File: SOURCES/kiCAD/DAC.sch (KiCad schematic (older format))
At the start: 196 parts, among them J16 MJ-519, J17 MJ-519, J20 MJ-519, J21 MJ-519, J24 Conn_01x06, J25 Conn_01x06, J27 Conn_01x06, J28 Conn_01x06, Q10 2SC3326, Q11 2SC3326, Q15 2SC3326, Q16 2SC3326, Q17 2SC3326, Q18 2SC3326, Q19 2SC3326, Q20 2SC3326, Q21 2SC3326, Q22 2SC3326, Q23 2SC3326, Q24 2SC3326, Q25 2SC3326, Q26 2SC3326, Q27 2SC3326, Q28 2SC3326, U14 PCM5102A, U16 PCM5102A, U17 PCM5102A, U18 PCM5102A, U20 OPA1632DR, U21 OPA1632DR, U22 OPA1632DR, U23 OPA1632DR, U24 OPA1632DR, U25 OPA1632DR, U26 OPA1632DR, U27 OPA1632DR

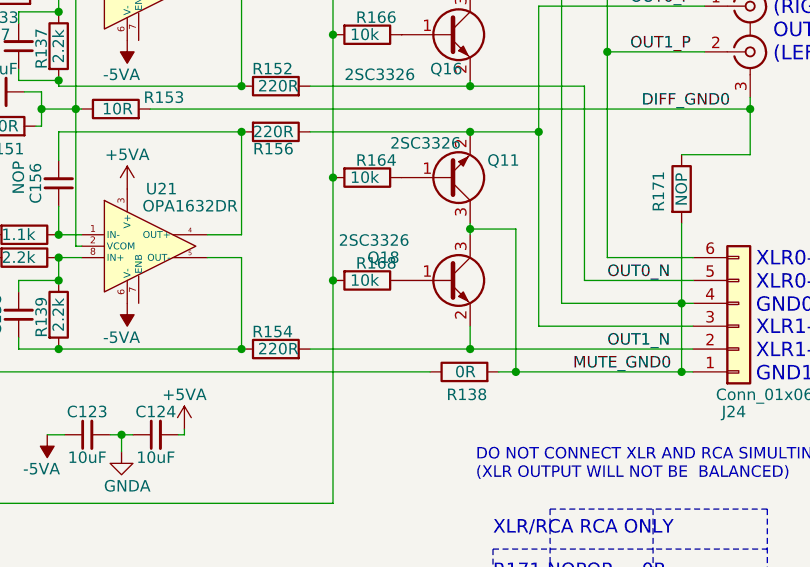
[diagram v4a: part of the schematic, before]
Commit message: Improved Coax Input Noise Immunities
Changed Coax input amp design and AC couling to EXOR
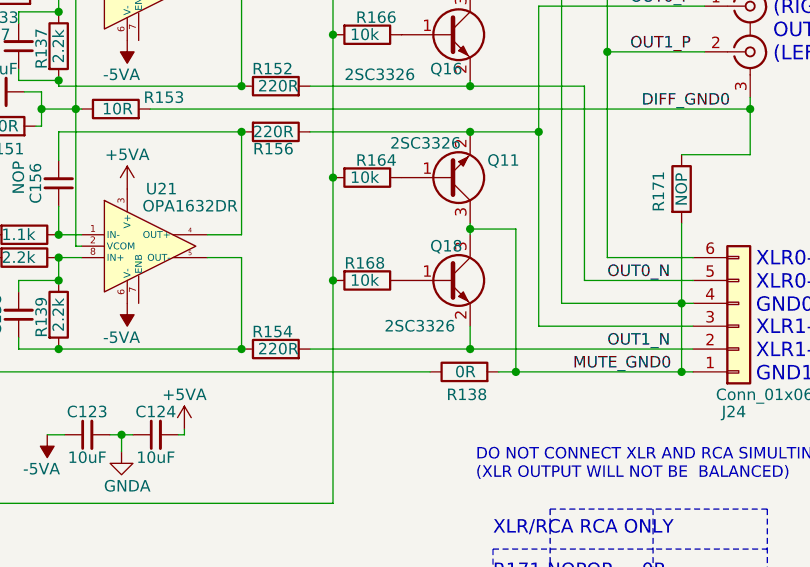
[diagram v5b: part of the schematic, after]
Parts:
- C114, C115, C116, C117, C96, C97, C98, C99: Description se Audio-Grade or Film Cap (ie. PML, ECHU, etc..) -> Use Audio-Grade or Film Cap (ie. PML, ECHU, etc..)
- C144, C146, C150, C151, C157, C158, C160, C161: Description use Audio-Grade or Film Cap (ie. PML, ECHU, etc..) -> Use Audio-Grade or Film Cap (ie. PML, ECHU, etc..); JLPCB# C363520 -> C525291
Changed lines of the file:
@@
 Title "FreeDSP OCTAVIA DAC part"
 Date "2023-07-22"
-Rev "0.3"
+Rev "0.32"
 Comp ""
 Comment1 ""
@@
 F 3 "~" H 11025 2875 50  0001 C CNN
 F 4 "C342877" H 11025 2875 50  0001 C CNN "JLPCB#"
-F 5 "se Audio-Grade or Film Cap (ie. PML, ECHU, etc..)" H 11025 2875 50  0001 C CNN "Description"
+F 5 "Use Audio-Grade or Film Cap (ie. PML, ECHU, etc..)" H 11025 2875 50  0001 C CNN "Description"
 	1    11025 2875
 	1    0    0    1
@@
 F 3 "~" H 11175 2875 50  0001 C CNN
 F 4 "C342877" H 11175 2875 50  0001 C CNN "JLPCB#"
-F 5 "se Audio-Grade or Film Cap (ie. PML, ECHU, etc..)" H 11175 2875 50  0001 C CNN "Description"
+F 5 "Use Audio-Grade or Film Cap (ie. PML, ECHU, etc..)" H 11175 2875 50  0001 C CNN "Description"
 	1    11175 2875
 	1    0    0    1
@@
 F 3 "~" H 3550 6900 50  0001 C CNN
 F 4 "C342877" H 3550 6900 50  0001 C CNN "JLPCB#"
-F 5 "se Audio-Grade or Film Cap (ie. PML, ECHU, etc..)" H 3550 6900 50  0001 C CNN "Description"
+F 5 "Use Audio-Grade or Film Cap (ie. PML, ECHU, etc..)" H 3550 6900 50  0001 C CNN "Description"
 	1    3550 6900
 	1    0    0    1
@@
 F 3 "~" H 3700 6900 50  0001 C CNN
 F 4 "C342877" H 3700 6900 50  0001 C CNN "JLPCB#"
-F 5 "se Audio-Grade or Film Cap (ie. PML, ECHU, etc..)" H 3700 6900 50  0001 C CNN "Description"
+F 5 "Use Audio-Grade or Film Cap (ie. PML, ECHU, etc..)" H 3700 6900 50  0001 C CNN "Description"
 	1    3700 6900
 	1    0    0    1
@@
 F 3 "~" H 11150 6775 50  0001 C CNN
 F 4 "C342877" H 11150 6775 50  0001 C CNN "JLPCB#"
-F 5 "se Audio-Grade or Film Cap (ie. PML, ECHU, etc..)" H 11150 6775 50  0001 C CNN "Description"
+F 5 "Use Audio-Grade or Film Cap (ie. PML, ECHU, etc..)" H 11150 6775 50  0001 C CNN "Description"
 	1    11150 6775
 	1    0    0    1
@@
 F 3 "~" H 11300 6775 50  0001 C CNN
 F 4 "C342877" H 11300 6775 50  0001 C CNN "JLPCB#"
-F 5 "se Audio-Grade or Film Cap (ie. PML, ECHU, etc..)" H 11300 6775 50  0001 C CNN "Description"
+F 5 "Use Audio-Grade or Film Cap (ie. PML, ECHU, etc..)" H 11300 6775 50  0001 C CNN "Description"
 	1    11300 6775
 	1    0    0    1
@@
 AR Path="/5D902CF8/656EA003" Ref="R?"  Part="1"
 AR Path="/5D902CF8/65D81CA2/656EA003" Ref="R168"  Part="1"
-F 0 "R168" V 5625 3925 50  0000 L CNN
+F 0 "R168" V 5625 3875 50  0000 L CNN
 F 1 "10k" V 5700 3900 50  0000 L CNN
 F 2 "Resistor_SMD:R_0603_1608Metric" V 5630 3975 50  0001 C CNN
@@
 U 1 1 65507B78
 P 6050 3975
-F 0 "Q18" H 5700 4075 50  0000 L CNN
-F 1 "2SC3326" H 5575 4150 50  0000 L CNN
+F 0 "Q18" H 5975 4125 50  0000 L CNN
+F 1 "2SC3326" H 5775 3775 50  0000 L CNN
 F 2 "Package_TO_SOT_SMD:SOT-23" H 6250 4075 50  0001 C CNN
 F 3 "~" H 6050 3975 50  0001 C CNN
@@
 F 3 "~" H 3350 3075 50  0001 C CNN
 F 4 "C342877" H 3350 3075 50  0001 C CNN "JLPCB#"
-F 5 "se Audio-Grade or Film Cap (ie. PML, ECHU, etc..)" H 3350 3075 50  0001 C CNN "Description"
+F 5 "Use Audio-Grade or Film Cap (ie. PML, ECHU, etc..)" H 3350 3075 50  0001 C CNN "Description"
 	1    3350 3075
 	1    0    0    1
@@
 F 2 "Capacitor_SMD:C_0805_2012Metric_Pad1.18x1.45mm_HandSolder" H 12275 6700 50  0001 C CNN
 F 3 "~" H 12275 6700 50  0001 C CNN
-F 4 "C363520" H 12275 6700 50  0001 C CNN "JLPCB#"
-F 5 "use Audio-Grade or Film Cap (ie. PML, ECHU, etc..)" H 12275 6700 50  0001 C CNN "Description"
+F 4 "C525291" H 12275 6700 50  0001 C CNN "JLPCB#"
+F 5 "Use Audio-Grade or Film Cap (ie. PML, ECHU, etc..)" H 12275 6700 50  0001 C CNN "Description"
 	1    12275 6700
 	1    0    0    1
@@
 F 2 "Capacitor_SMD:C_0805_2012Metric_Pad1.18x1.45mm_HandSolder" H 12350 7850 50  0001 C CNN
 F 3 "~" H 12350 7850 50  0001 C CNN
-F 4 "C363520" H 12350 7850 50  0001 C CNN "JLPCB#"
-F 5 "use Audio-Grade or Film Cap (ie. PML, ECHU, etc..)" H 12350 7850 50  0001 C CNN "Description"
+F 4 "C525291" H 12350 7850 50  0001 C CNN "JLPCB#"
+F 5 "Use Audio-Grade or Film Cap (ie. PML, ECHU, etc..)" H 12350 7850 50  0001 C CNN "Description"
 	1    12350 7850
 	1    0    0    1
@@
 F 2 "Capacitor_SMD:C_0805_2012Metric_Pad1.18x1.45mm_HandSolder" H 12000 2800 50  0001 C CNN
 F 3 "~" H 12000 2800 50  0001 C CNN
-F 4 "C363520" H 12000 2800 50  0001 C CNN "JLPCB#"
-F 5 "use Audio-Grade or Film Cap (ie. PML, ECHU, etc..)" H 12000 2800 50  0001 C CNN "Description"
+F 4 "C525291" H 12000 2800 50  0001 C CNN "JLPCB#"
+F 5 "Use Audio-Grade or Film Cap (ie. PML, ECHU, etc..)" H 12000 2800 50  0001 C CNN "Description"
 	1    12000 2800
 	1    0    0    1
@@
 F 2 "Capacitor_SMD:C_0805_2012Metric_Pad1.18x1.45mm_HandSolder" H 12075 4050 50  0001 C CNN
 F 3 "~" H 12075 4050 50  0001 C CNN
-F 4 "C363520" H 12075 4050 50  0001 C CNN "JLPCB#"
-F 5 "use Audio-Grade or Film Cap (ie. PML, ECHU, etc..)" H 12075 4050 50  0001 C CNN "Description"
+F 4 "C525291" H 12075 4050 50  0001 C CNN "JLPCB#"
+F 5 "Use Audio-Grade or Film Cap (ie. PML, ECHU, etc..)" H 12075 4050 50  0001 C CNN "Description"
 	1    12075 4050
 	1    0    0    1
@@
 F 3 "~" H 3200 3075 50  0001 C CNN
 F 4 "C342877" H 3200 3075 50  0001 C CNN "JLPCB#"
-F 5 "se Audio-Grade or Film Cap (ie. PML, ECHU, etc..)" H 3200 3075 50  0001 C CNN "Description"
+F 5 "Use Audio-Grade or Film Cap (ie. PML, ECHU, etc..)" H 3200 3075 50  0001 C CNN "Description"
 	1    3200 3075
 	1    0    0    1
@@
 F 2 "Capacitor_SMD:C_0805_2012Metric_Pad1.18x1.45mm_HandSolder" H 4175 4125 50  0001 C CNN
 F 3 "~" H 4175 4125 50  0001 C CNN
-F 4 "C363520" H 4175 4125 50  0001 C CNN "JLPCB#"
-F 5 "use Audio-Grade or Film Cap (ie. PML, ECHU, etc..)" H 4175 4125 50  0001 C CNN "Description"
+F 4 "C525291" H 4175 4125 50  0001 C CNN "JLPCB#"
+F 5 "Use Audio-Grade or Film Cap (ie. PML, ECHU, etc..)" H 4175 4125 50  0001 C CNN "Description"
 	1    4175 4125
 	1    0    0    1
@@
 F 2 "Capacitor_SMD:C_0805_2012Metric_Pad1.18x1.45mm_HandSolder" H 4175 2950 50  0001 C CNN
 F 3 "~" H 4175 2950 50  0001 C CNN
-F 4 "C363520" H 4175 2950 50  0001 C CNN "JLPCB#"
-F 5 "use Audio-Grade or Film Cap (ie. PML, ECHU, etc..)" H 4175 2950 50  0001 C CNN "Description"
+F 4 "C525291" H 4175 2950 50  0001 C CNN "JLPCB#"
+F 5 "Use Audio-Grade or Film Cap (ie. PML, ECHU, etc..)" H 4175 2950 50  0001 C CNN "Description"
 	1    4175 2950
 	1    0    0    1
@@
 F 2 "Capacitor_SMD:C_0805_2012Metric_Pad1.18x1.45mm_HandSolder" H 4625 6850 50  0001 C CNN
 F 3 "~" H 4625 6850 50  0001 C CNN
-F 4 "C363520" H 4625 6850 50  0001 C CNN "JLPCB#"
-F 5 "use Audio-Grade or Film Cap (ie. PML, ECHU, etc..)" H 4625 6850 50  0001 C CNN "Description"
+F 4 "C525291" H 4625 6850 50  0001 C CNN "JLPCB#"
+F 5 "Use Audio-Grade or Film Cap (ie. PML, ECHU, etc..)" H 4625 6850 50  0001 C CNN "Description"
 	1    4625 6850
 	1    0    0    1
@@
 F 2 "Capacitor_SMD:C_0805_2012Metric_Pad1.18x1.45mm_HandSolder" H 4675 8150 50  0001 C CNN
 F 3 "~" H 4675 8150 50  0001 C CNN
-F 4 "C363520" H 4675 8150 50  0001 C CNN "JLPCB#"
-F 5 "use Audio-Grade or Film Cap (ie. PML, ECHU, etc..)" H 4675 8150 50  0001 C CNN "Description"
+F 4 "C525291" H 4675 8150 50  0001 C CNN "JLPCB#"
+F 5 "Use Audio-Grade or Film Cap (ie. PML, ECHU, etc..)" H 4675 8150 50  0001 C CNN "Description"
 	1    4675 8150
 	1    0    0    1

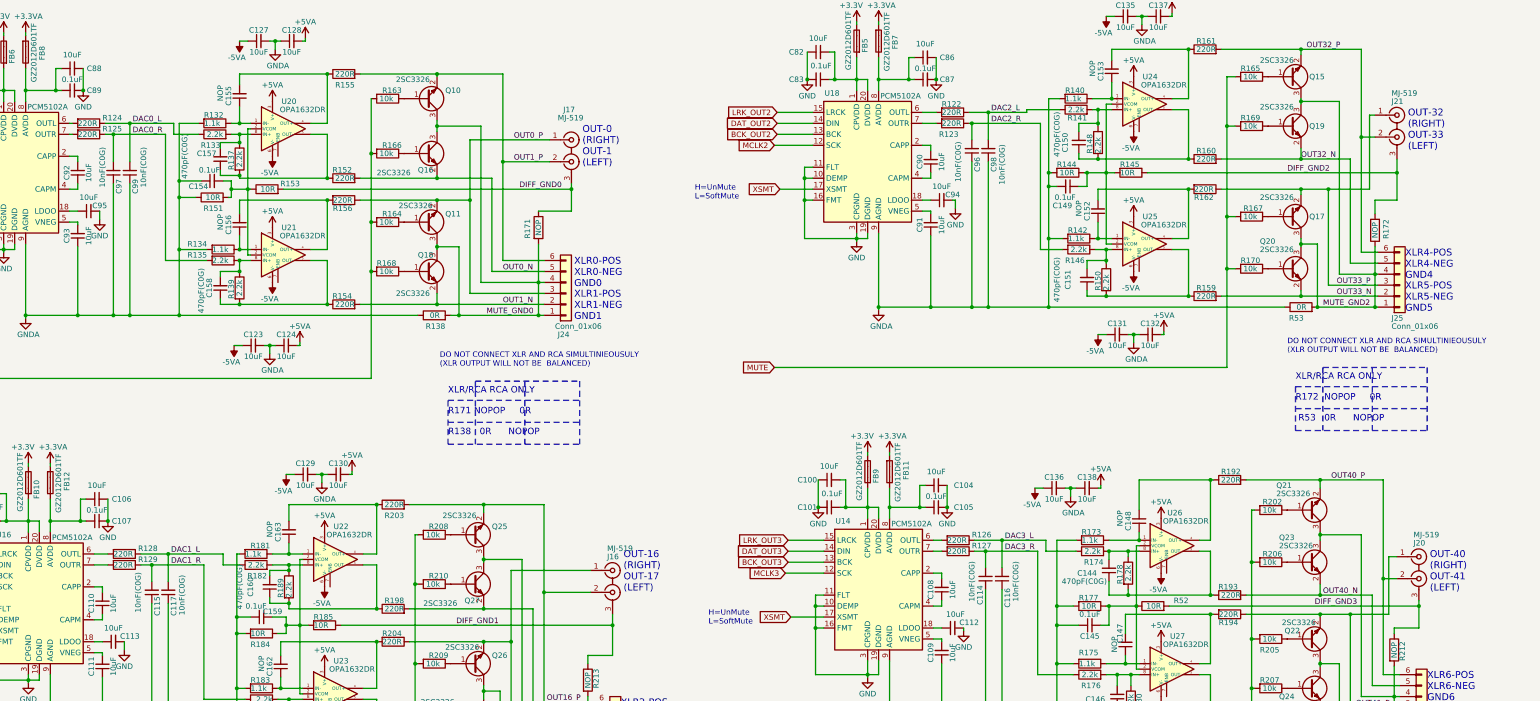
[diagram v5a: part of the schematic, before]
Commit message: Voltage Regulator Changed to LM317
PCB layout is also updated in some of the places.
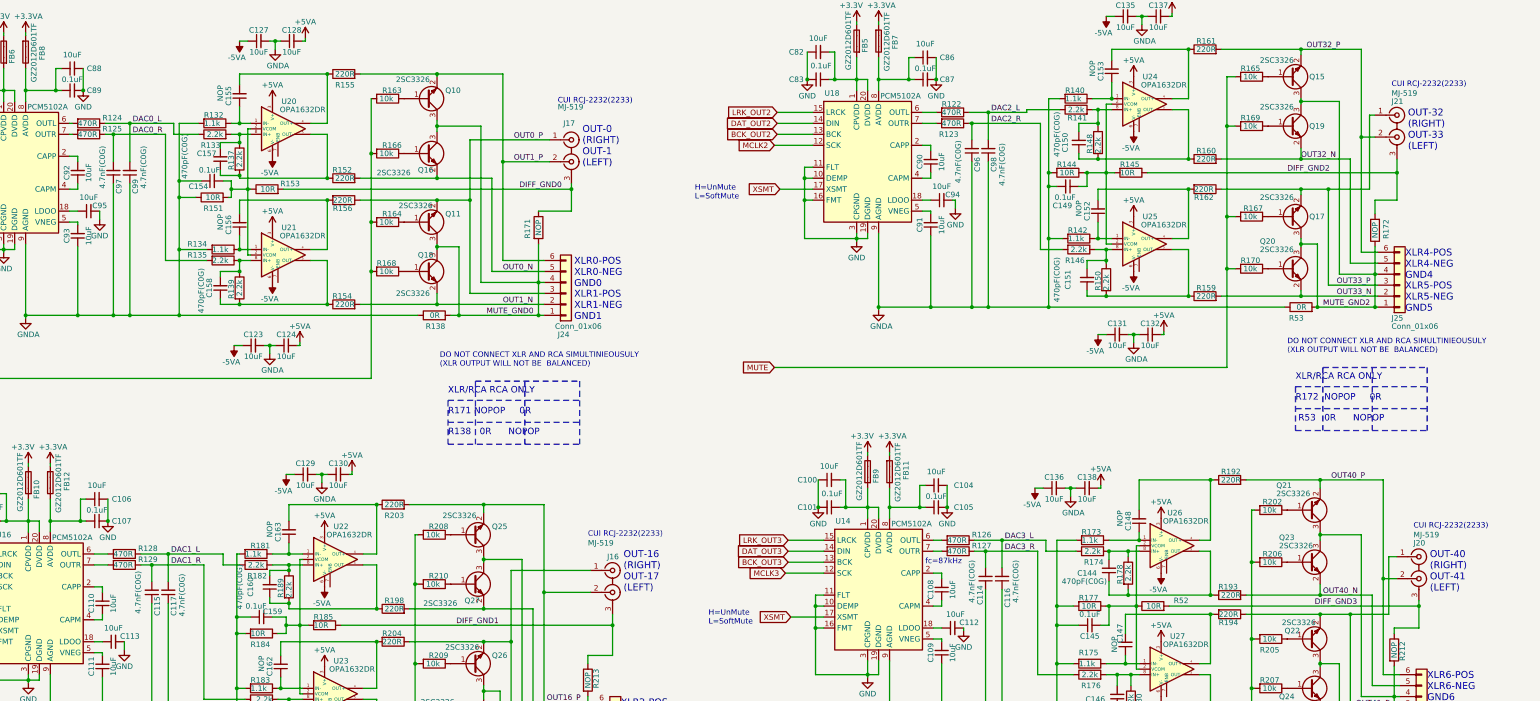
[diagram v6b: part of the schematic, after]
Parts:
- C114, C115, C116, C117, C96, C97, C98, C99: value 10nF(C0G) -> 4.7nF(C0G); Description Use Audio-Grade or Film Cap (ie. PML, ECHU, etc..) -> Better Use Audio-Grade or Film Cap (ie. PML, ECHU, etc..); JLPCB# C342877 -> C880299
- C144, C146, C150, C151, C157, C158, C160, C161: Description Use Audio-Grade or Film Cap (ie. PML, ECHU, etc..) -> Better Use Audio-Grade or Film Cap (ie. PML, ECHU, etc..)
- C147, C148, C152, C153, C155, C156, C162, C163: Description (none) -> Prepared for just in case
- J16, J17, J20, J21: Description (none) -> Vertical Stereo RCA-pin Jack (Upper=Left, Lower=Right) RCJ-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
- Q10, Q11, Q15, Q16, Q17, Q18, Q19, Q20, Q21, Q22, Q23, Q24, Q25, Q26, Q27, Q28: Description alt. 2SC4213 or 2SD2704 -> alt. 2SC4213 or 2SD2704 (Audio Muting)
- R122, R123, R124, R125, R126, R127, R128, R129: value 220R -> 470R; JLPCB# C22962 -> C23179
- U14, U16, U17, U18: Description (none) -> 32bit Audio DAC
- U20, U21, U22, U23, U24, U25, U26, U27: Description (none) -> for Balanced/Differential Output driver
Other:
- note added: "CUI RCJ-2232(2233)"
- note added: "fc=87kHz"
